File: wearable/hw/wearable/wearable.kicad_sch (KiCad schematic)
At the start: 103 parts, among them IC1 LM4041CILPR, J2 Conn_02x05_Odd_Even, J3 Interrupts, J4 Data, J5 Data, J8 USBC Charger, SW1 SW_Toggle, U1 LT3042xMSE, U2 BNO080, U3 nRF54L15-QFXX, U4 MAX77659AENV+, U5 ADS1299IPAG, Y1 32MHz, Y2 32.768kHz, Y3 32.768kHz

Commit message: More layout progress and some fun stuff
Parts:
- renumbered TP3 to TP1, TP1 to TP3
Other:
- moved on the sheet: TP1, TP3
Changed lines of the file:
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@@
 	(wire
 		(pts
-			(xy 222.25 22.86) (xy 223.52 22.86)
+			(xy 222.25 24.765) (xy 223.52 24.765)
 		)
 		(stroke
@@
 	(wire
 		(pts
-			(xy 222.25 17.78) (xy 223.52 17.78)
+			(xy 222.25 15.24) (xy 223.52 15.24)
 		)
 		(stroke
@@
 	(global_label "AMUX"
 		(shape input)
-		(at 223.52 22.86 0)
+		(at 223.52 24.765 0)
 		(fields_autoplaced yes)
 		(effects
@@
 		)
 		(property "Intersheetrefs" "${INTERSHEET_REFS}"
-			(at 231.5852 22.86 0)
+			(at 231.5852 24.765 0)
 			(effects
 				(font
@@
 	(global_label "AVDD"
 		(shape input)
-		(at 223.52 17.78 0)
+		(at 223.52 15.24 0)
 		(fields_autoplaced yes)
 		(effects
@@
 		)
 		(property "Intersheetrefs" "${INTERSHEET_REFS}"
-			(at 231.2224 17.78 0)
+			(at 231.2224 15.24 0)
 			(effects
 				(font
@@
 	(symbol
 		(lib_id "Connector:TestPoint")
-		(at 222.25 17.78 90)
+		(at 222.25 15.24 90)
 		(unit 1)
 		(exclude_from_sim no)
@@
 		(on_board yes)
 		(dnp no)
-		(property "Reference" "TP3"
-			(at 218.948 12.7 90)
+		(property "Reference" "TP1"
+			(at 218.948 10.16 90)
 			(effects
 				(font
@@
 		)
 		(property "Value" "AVDD"
-			(at 218.948 15.494 90)
+			(at 218.948 12.954 90)
 			(effects
 				(font
@@
 		)
 		(property "Footprint" "TestPoint:TestPoint_Bridge_Pitch2.0mm_Drill0.7mm"
-			(at 222.25 12.7 0)
+			(at 222.25 10.16 0)
 			(effects
 				(font
@@
 		)
 		(property "Datasheet" "~"
-			(at 222.25 12.7 0)
+			(at 222.25 10.16 0)
 			(effects
 				(font
@@
 		)
 		(property "Description" "test point"
-			(at 222.25 17.78 0)
+			(at 222.25 15.24 0)
 			(effects
 				(font
@@
 			(project "wearable"
 				(path "/eeafcd59-7fa6-43d8-bb03-b6b192c7124f"
-					(reference "TP3")
+					(reference "TP1")
 					(unit 1)
 				)
@@
 	(symbol
 		(lib_id "Connector:TestPoint")
-		(at 222.25 22.86 90)
+		(at 222.25 24.765 90)
 		(unit 1)
 		(exclude_from_sim no)
@@
 		(on_board yes)
 		(dnp no)
-		(property "Reference" "TP1"
-			(at 218.948 17.78 90)
+		(property "Reference" "TP3"
+			(at 218.948 19.685 90)
 			(effects
 				(font
@@
 		)
 		(property "Value" "BatteryStatus"
-			(at 218.948 20.574 90)
+			(at 218.948 22.479 90)
 			(effects
 				(font
@@
 		)
 		(property "Footprint" "TestPoint:TestPoint_Bridge_Pitch2.0mm_Drill0.7mm"
-			(at 222.25 17.78 0)
+			(at 222.25 19.685 0)
 			(effects
 				(font
@@
 		)
 		(property "Datasheet" "~"
-			(at 222.25 17.78 0)
+			(at 222.25 19.685 0)
 			(effects
 				(font
@@
 		)
 		(property "Description" "test point"
-			(at 222.25 22.86 0)
+			(at 222.25 24.765 0)
 			(effects
 				(font
@@
 			(project ""
 				(path "/eeafcd59-7fa6-43d8-bb03-b6b192c7124f"
-					(reference "TP1")
+					(reference "TP3")
 					(unit 1)
 				)

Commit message: Some more changes
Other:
- note added: "EEG Inputs"
- note removed: "EEG Inputs (TODO: Add filters)"
- note removed: "We need to make this 5V signal cleaner"
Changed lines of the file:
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@@
 		)
 	)
-	(text "EEG Inputs (TODO: Add filters)"
+	(text "EEG Inputs\n"
 		(exclude_from_sim no)
-		(at 245.872 206.756 0)
+		(at 209.296 164.084 0)
 		(effects
 			(font
@@
 		)
 	)
-	(text "We need to make this 5V signal cleaner"
-		(exclude_from_sim no)
-		(at 201.422 216.916 0)
-		(effects
-			(font
-				(size 1.27 1.27)
-			)
-		)
-	)

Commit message: Some stuff
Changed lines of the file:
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@@
 	(text "TODO: layout the RF signal"
 		(exclude_from_sim no)
-		(at 157.226 120.142 0)
+		(at 147.828 121.666 0)
 		(effects
 			(font
@@
 	(wire
 		(pts
-			(xy 150.495 123.825) (xy 162.56 123.825)
-		)
-		(stroke
-			(width 0)
-			(type default)
-		)
-	)
-	(wire
-		(pts
 			(xy 52.07 267.335) (xy 62.23 267.335)
 		)
@@
 	(wire
 		(pts
+			(xy 150.495 123.825) (xy 160.655 123.825)
+		)
+		(stroke
+			(width 0)
+			(type default)
+		)
+	)
+	(wire
+		(pts
 			(xy 106.045 294.005) (xy 106.045 291.465)
 		)
@@
 	(global_label "RF"
 		(shape input)
-		(at 162.56 123.825 0)
+		(at 160.655 123.825 0)
 		(fields_autoplaced yes)
 		(effects
@@
 		)
 		(property "Intersheetrefs" "${INTERSHEET_REFS}"
-			(at 167.9038 123.825 0)
+			(at 165.9988 123.825 0)
 			(effects
 				(font

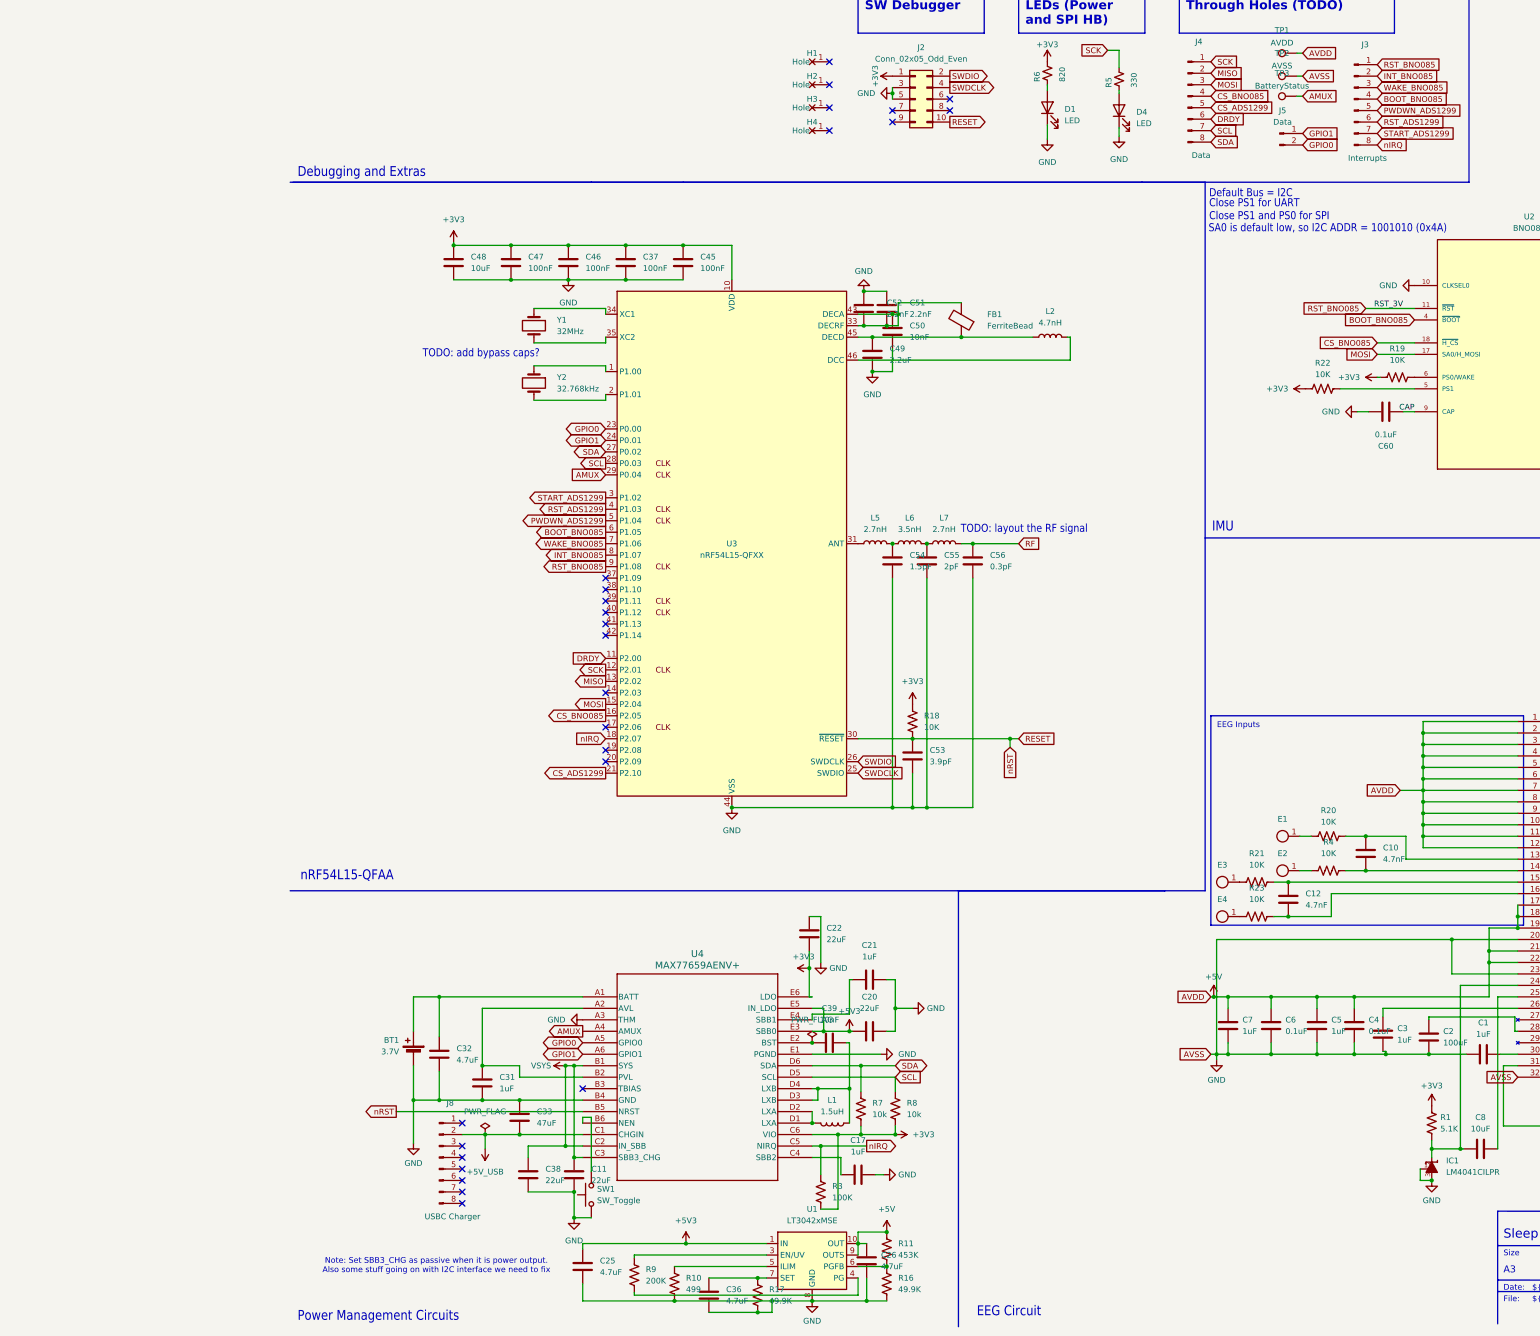
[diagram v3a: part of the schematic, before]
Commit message: Significant layout progress
NOTE: We will need to rework the power management portion of the schematic due to layout issues
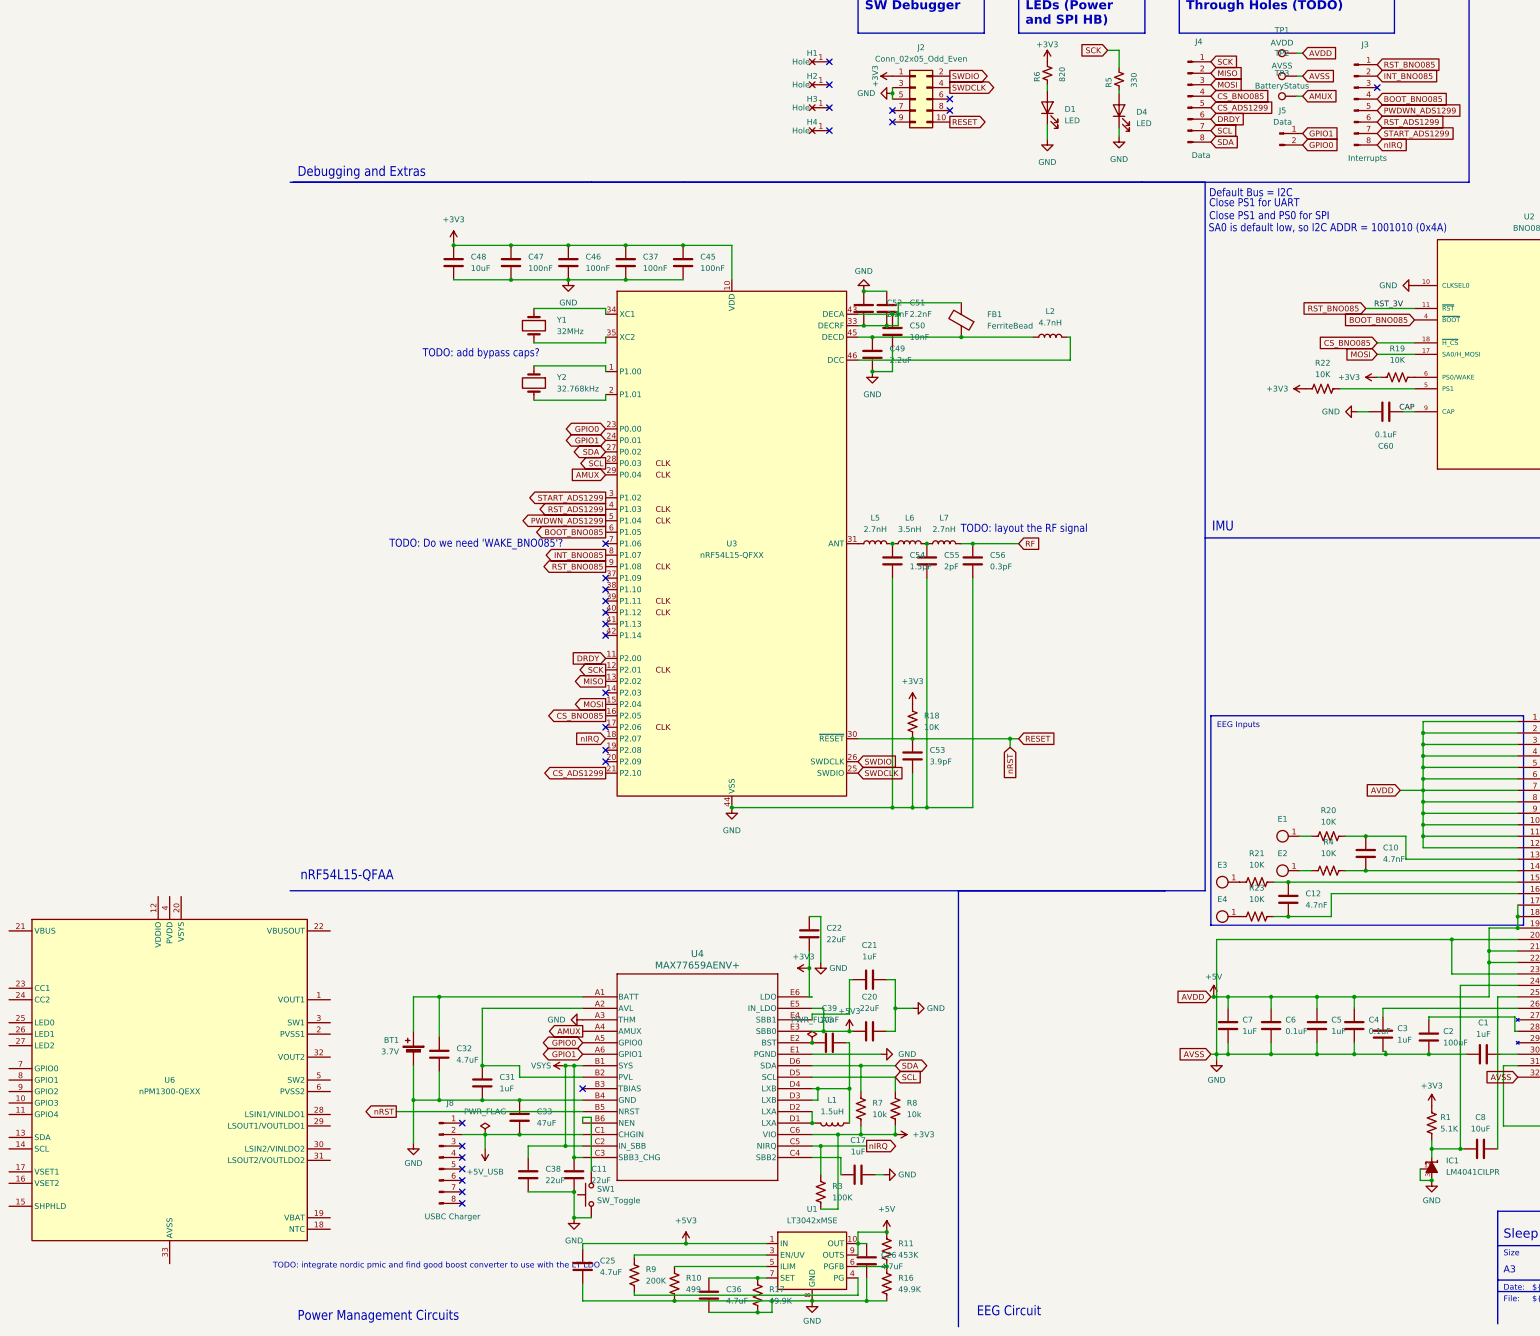
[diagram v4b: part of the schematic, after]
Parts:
- added U6: nPM1300-QEXX, Package_DFN_QFN:QFN-32-1EP_5x5mm_P0.5mm_EP3.6x3.6mm_ThermalVias, symbol PCM_nordic-lib-kicad-npm:nPM1300-QEXX
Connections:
- net WAKE_BNO085: no longer names the net of U3.7 (P1.06)
- net WAKE_BNO085: no longer J3.3 (Pin_3)
- no-connect marks 32 -> 34
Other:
- note added: "TODO: Do we need 'WAKE_BNO085'?"
- note added: "TODO: integrate nordic pmic and find good boost converter to use with the LT LDO"
- note removed: "Note: Set SBB3_CHG as passive when it is power output. Also some stuff going on with I2C interface we need to fix"
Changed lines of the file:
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@@
 		)
 	)
+	(text "TODO: Do we need 'WAKE_BNO085'?"
+		(exclude_from_sim no)
+		(at 21.336 124.968 0)
+		(effects
+			(font
+				(size 1.778 1.5113)
+			)
+			(justify left bottom)
+		)
+	)
 	(text "Keep as close to 2.5V as possible?"
 		(exclude_from_sim no)
@@
 		)
 	)
-	(text "Note: Set SBB3_CHG as passive when it is power output. \nAlso some stuff going on with I2C interface we need to fix"
+	(text "TODO: integrate nordic pmic and find good boost converter to use with the LT LDO"
 		(exclude_from_sim no)
 		(at 31.75 283.718 0)
@@
 	)
 	(no_connect
+		(at 240.03 22.86)
+	)
+	(no_connect
 		(at 69.215 139.065)
 	)
@@
 	)
 	(no_connect
-		(at 69.215 133.985)
-	)
-	(no_connect
 		(at 145.415 25.4)
 	)
@@
 	)
 	(no_connect
+		(at 69.215 123.825)
+	)
+	(no_connect
 		(at 69.215 144.145)
 	)
@@
 	)
 	(no_connect
+		(at 69.215 133.985)
+	)
+	(no_connect
 		(at 342.265 221.615)
 	)
@@
 		)
 	)
-	(global_label "WAKE_BNO085"
-		(shape input)
-		(at 240.03 22.86 0)
-		(fields_autoplaced yes)
-		(effects
-			(font
-				(size 1.27 1.27)
-			)
-			(justify left)
-		)
-		(property "Intersheetrefs" "${INTERSHEET_REFS}"
-			(at 256.5013 22.86 0)
-			(effects
-				(font
-					(size 1.27 1.27)
-				)
-				(justify left)
-				(hide yes)
-			)
-		)
-	)
 	(global_label "MOSI"
 		(shape output)
@@
 		)
 	)
-	(global_label "WAKE_BNO085"
-		(shape output)
-		(at 69.215 123.825 180)
-		(fields_autoplaced yes)
-		(effects
-			(font
-				(size 1.27 1.27)
-			)
-			(justify right)
-		)
-		(property "Intersheetrefs" "${INTERSHEET_REFS}"
-			(at 52.7437 123.825 0)
-			(effects
-				(font
-					(size 1.27 1.27)
-				)
-				(justify right)
-				(hide yes)
-			)
-		)
-	)
 	(global_label "START_ADS1299"
 		(shape output)
@@
 					(unit 1)
 				)
+			)
+		)
+	)
+	(symbol
+		(lib_id "PCM_nordic-lib-kicad-npm:nPM1300-QEXX")
+		(at -27.305 242.57 0)
+		(unit 1)
+		(exclude_from_sim no)
+		(in_bom yes)
+		(on_board yes)
+		(dnp no)
+		(fields_autoplaced yes)
+		(property "Reference" "U6"
+			(at -27.305 242.57 0)
+			(do_not_autoplace yes)
+			(effects
+				(font
+					(size 1.27 1.27)
+				)
+			)
+		)
+		(property "Value" "nPM1300-QEXX"
+			(at -27.305 245.11 0)
+			(do_not_autoplace yes)
+			(effects
+				(font
+					(size 1.27 1.27)
+				)
+			)
+		)
+		(property "Footprint" "Package_DFN_QFN:QFN-32-1EP_5x5mm_P0.5mm_EP3.6x3.6mm_ThermalVias"
+			(at -27.305 300.99 0)
+			(effects
+				(font
+					(size 1.27 1.27)
+				)
+				(hide yes)
+			)
+		)
+		(property "Datasheet" "https://docs.nordicsemi.com/bundle/ps_npm1300"
+			(at -27.305 298.45 0)
+			(effects
+				(font
+					(size 1.27 1.27)
+				)
+				(hide yes)
+			)
+		)
+		(property "Description" "PMIC, LED Driver, Battery Charger, QFN-32"
+			(at -27.305 295.91 0)
+			(effects
+				(font
+					(size 1.27 1.27)
+				)
+				(hide yes)
+			)
+		)
+		(pin "21"
+		)
+		(pin "23"
+		)
+		(pin "24"
+		)
+		(pin "25"
+		)
+		(pin "26"
+		)
+		(pin "27"
+		)
+		(pin "16"
+		)
+		(pin "3"
+		)
+		(pin "4"
+		)
+		(pin "18"
+		)
+		(pin "13"
+		)
+		(pin "20"
+		)
+		(pin "5"
+		)
+		(pin "14"
+		)
+		(pin "1"
+		)
+		(pin "10"
+		)
+		(pin "11"
+		)
+		(pin "17"
+		)
+		(pin "32"
+		)
+		(pin "29"
+		)
+		(pin "12"
+		)
+		(pin "22"
+		)
+		(pin "30"
+		)
+		(pin "15"
+		)
+		(pin "9"
+		)
+		(pin "7"
+		)
+		(pin "8"
+		)
+		(pin "33"
+		)
+		(pin "31"
+		)
+		(pin "19"
+		)
+		(pin "28"
+		)
+		(pin "6"
+		)
+		(pin "2"
+		)
+		(instances
+			(project ""
+				(path "/eeafcd59-7fa6-43d8-bb03-b6b192c7124f"
+					(reference "U6")
+					(unit 1)
+				)
